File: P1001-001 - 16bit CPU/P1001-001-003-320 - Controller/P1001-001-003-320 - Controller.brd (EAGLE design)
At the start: 200 x 48 mm, 108 parts, among them IC1 74LS138D, IC10 74ALS00D, IC11 74ABT164D, IC12 74ABT164D, IC13 74ABT164D, IC14 74LS138D, IC15 74ABT164D, IC16 74ABT164D, IC17 74ABT164D, IC18 74ABT164D, IC19 74ABT164D, IC2 74LS157D, IC20 74ABT164D, IC3 74LS138D, IC4 74LS138D, IC5 74LS138D, IC6 74LS157D, IC7 74LS157D, IC8 74LS157D, IC9 74LS157D, J1 22-27-2041-04

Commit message: Add the control board
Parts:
- removed ALU_HIGH, ALU_LOW, A_OUT2, B_IN_LOW, B_OUT2, C_REG, RAN_IN_2, STACK: (no value), jumper:JP4
- removed A_CLEAR, B_CLEAR, D_IN, RAM_IN_LOW, X_SWAP: (no value), led:SFH482
- removed BACKBUS, FRONTBUS: (no value), con-harting-ml:ML16
- removed B_IN_HIGH, RAM_PC_OUT, RAN_IN_3: (no value), jumper:JP1
- removed D_REG, RAN_IN_1, X_REG: (no value), jumper:JP2W
- removed IC11, IC12, IC13, IC15, IC16, IC17, IC18, IC19, IC20: 74ABT164D, 74xx-us:SO14
- removed IC14: 74LS138D, 74xx-us:SO16
- removed IC2, IC6, IC7, IC8, IC9: 74LS157D, 74xx-us:SO16
- removed JP5: (no value), jumper:JP2
- removed U$2, U$3: SST39VF1602-70-4I-EKE, 16bit:TSOP48
- added ABC_CLEAR, B_IN_LOW1, HALT_RESEDT_NEXTINS, PC_MAR_IR_IN, RAM_STACK_IN: (no value), jumper:JP2W
- added ADD_HIGH, ADD_LOW, ADD_MID, BA_HIGH, BA_LOW, BB_HIGH, BB_LOW, BC_HIGH, BC_LOW: 74ABT164D, 74xx-us:SO14
- added ADD_SUB, B_IN_HIGH1, CLEAR_OUNS, EXTRA_1_2_PINS, EXTRA_3_4_PINS, EXTRA_5_6_PINS, INTERUPTS, PC_INC_DEC, RAM_IMT_OUT: (no value), jumper:JP1
- added A_CLEAR_LED, B_CLEAR_LED, D_CLEAR_LED, D_HIGH, D_IN_H, D_IN_L, D_LOW, EXTRA1, EXTRA2, EXTRA3, EXTRA4, EXTRA5, EXTRA6, EXTRA_OUT1, EXTRA_OUT2, EXTRA_OUT3, EXTRA_OUT4, INTERUPT_OUT, PAUSE_INERUPT, PC_DEC, PLAY_INTERUPT, RAM_IN_L, ROL, ROR, STEP1, STEP2, STEP3, STEP4: (no value), led:SFH482
- added A_OUT_PINS, B_OUT_PIMS, C_X_OC_STACK_OUT, D_OUT_PINS, EXTRA_OUT, IN_C_D_X, LOGIC_OP, SHIFT_ROLL, STACK_C, STEP_PINS: (no value), jumper:JP4
- added BANKA, BANKB, BANKC: SST39VF1602-70-4I-EKE, 16bit:TSOP48
- added IC21, IC22, IC23: 74LS138D, 74xx-us:SO16
- added IC27: MEGA8535-A, atmel:TQFP44
- added POWER_PINS, READ_WRITE: (no value), jumper:JP2
- added PULL_DOWN, R12, R13, R14: (no value), rcl:M0805
- added R10, R7, R8: (no value), resistor-bourns:SO16
- added RN2: (no value), resistor-dil:SOMC20
- added SV3: (no value), con-harting-ml:ML16
- added SV5: (no value), con-harting-ml:ML6
- added SW_PROD_1, SW_PROD_2, SW_PROD_3, SW_PROD_4, SW_PROD_5: 74LS157D, 74xx-us:SO16
- A_IN_LOW: device jumper:JP4 -> jumper:JP2W
- JP4: device jumper:JP1 -> jumper:JP3Q
- U$1: value SST39VF1602-70-4I-EKE -> 4-DIGIT-7-SEGMENT; device 16bit:TSOP48 -> ADAFRUIT:4-DIGIT-7-SEGMENT
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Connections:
- removed net A-CLEAR: A_CLEAR.K, A_IN_LOW.4, IC14.15
- removed net ADD: ADD.K, ALU_LOW.1, IC3.15
- removed net AND: ALU_HIGH.3, AND.K, IC3.9
- removed net A_HIGH: A_HIGH.K, A_OUT2.2, IC5.14
- removed net A_IN: A_IN.K, A_IN_LOW.3, IC14.14
- removed net A_IN_H_H: A_IN_H_H.K, A_IN_LOW.1, IC14.12
- removed net A_IN_H_L: A_IN_HIGH.1, A_IN_H_L.K, IC14.10
- removed net A_IN_L_H: A_IN_HIGH.2, A_IN_L_H.K, IC14.11
- removed net A_IN_L_L: A_IN_LOW.2, A_IN_L_L.K, IC14.13
- removed net A_LOW: A_LOW.K, A_OUT2.3, IC5.13
- removed net A_OUT: A_OUT.K, A_OUT2.4, IC5.12
- removed net A_SWAP: A_OUT2.1, A_SWAP.K, IC5.15
- removed net BUS0: BACKBUS.1, IC4.1, IC5.1
- removed net BUS1: BACKBUS.2, IC4.2, IC5.2
- removed net BUS10: BACKBUS.11, C_IN.K, C_REG.1
- removed net BUS11: BACKBUS.12, D_IN.K, D_REG.1
- removed net BUS12: BACKBUS.13, X_IN.K, X_REG.1
- removed net BUS13: BACKBUS.14, IR_IN.K, RAN_IN_3.2
- removed net BUS14: BACKBUS.15, MAR_IN.K, RAN_IN_3.1
- removed net BUS15: BACKBUS.16, PC_IN.K, RAN_IN_2.4
- removed net BUS16: FRONTBUS.1, RAM_IN_LOW.K, RAN_IN_2.3
- removed net BUS17: FRONTBUS.2, RAM_IN_H.K, RAN_IN_2.2
- removed net BUS18: FRONTBUS.3, IC3.1
- removed net BUS19: FRONTBUS.4, IC3.2
- removed net BUS2: BACKBUS.3, IC4.3, IC5.3
- removed net BUS20: FRONTBUS.5, IC3.3
- removed net BUS21: FRONTBUS.6, PC_INC.K, RAN_IN_2.1
- removed net BUS22: FRONTBUS.7, STACK.2, STACK_INC.K
- removed net BUS23: FRONTBUS.8, STACK.3, STACK_DEC.K
- removed net BUS24: C_INC.K, C_REG.2, FRONTBUS.9
- removed net BUS25: C_DEC.K, C_REG.3, FRONTBUS.10
- removed net BUS26: FRONTBUS.11, RAN_IN_1.3, RESET.K
- removed net BUS27: FRONTBUS.12, HALT.K, RAN_IN_1.2
- removed net BUS28: FRONTBUS.13, NEXT_INS.K, RAN_IN_1.1
- removed net BUS29: FRONTBUS.14, STACK.1, STACK_IN.K
- removed net BUS3: BACKBUS.4, IC4.4, IC5.4
- removed net BUS30: FRONTBUS.15
- removed net BUS31: FRONTBUS.16
- removed net BUS4: BACKBUS.5, IC14.1
- removed net BUS5: BACKBUS.6, IC14.2
- removed net BUS6: BACKBUS.7, IC14.3
- removed net BUS7: BACKBUS.8, IC1.1
- removed net BUS8: BACKBUS.9, IC1.2
- removed net BUS9: BACKBUS.10, IC1.3
- removed net B_CLEAR: B_CLEAR.K, B_IN_LOW.4, IC1.15
- removed net B_HIGH: B_HIGH.K, B_OUT2.2, IC5.10
- removed net B_IN: B_IN.K, B_IN_LOW.3, IC1.14
- removed net B_IN_H_H: B_IN_H_H.K, B_IN_LOW.1, IC1.12
- removed net B_IN_H_L: B_IN_HIGH.1, B_IN_H_L.K, IC1.10
- removed net B_IN_L_H: B_IN_HIGH.2, B_IN_L_H.K, IC1.11
- removed net B_IN_L_L: B_IN_LOW.2, B_IN_L_L.K, IC1.13
- removed net B_LOW: B_LOW.K, B_OUT2.3, IC5.9
- removed net B_OUT: B_OUT.K, B_OUT2.4, IC5.7
- removed net B_SWAP: B_OUT2.1, B_SWAP.K, IC5.11
- removed net HALT_LED: NEXT_INS.A, R3.13
- removed net NOT: ALU_HIGH.1, IC3.11, NOT.K
- removed net OR: ALU_HIGH.2, IC3.10, OR.K
- removed net PC_OUT: IC4.14, PC_OUT.K
- removed net RAM_OUT: IC4.9, RAM_OUT.K
- removed net SHL: ALU_LOW.3, IC3.13, SHL.K
- removed net SHR: ALU_LOW.4, IC3.12, SHR.K
- removed net SUB: ALU_LOW.2, IC3.14, SUB.K
- removed net XOR: ALU_HIGH.4, IC3.7, XOR.K
- new net A: IC27.37, RN2.20
- new net B: IC27.36, RN2.19
- new net BANKA_PROG: BANKA.11, JP4.5, R12.1
- new net BANKB_PROG: BANKB.11, JP4.3, R13.1
- new net BANKC_PROG: BANKC.11, JP4.1, R14.1
- new net C: IC27.35, RN2.18
- new net D: IC27.34, RN2.17
- new net DIG0: IC27.40, U$1.PIN14
- new net DIG1: IC27.41, U$1.PIN11
- new net DIG2: IC27.42, U$1.PIN10
- new net DIG3: IC27.43, U$1.PIN6
- new net DP: IC27.30, RN2.13
- new net E: IC27.33, RN2.16
- new net EXTERN_BUS0: IC27.9, R10.1, SV3.1
- new net EXTERN_BUS1: IC27.10, R10.9, SV3.2
- new net EXTERN_BUS10: IC27.21, R10.6, SV3.11
- new net EXTERN_BUS11: IC27.22, R10.14, SV3.12
- new net EXTERN_BUS12: IC27.23, R10.7, SV3.13
- new net EXTERN_BUS13: IC27.24, R10.15, SV3.14
- new net EXTERN_BUS14: IC27.25, R10.8, SV3.15
- new net EXTERN_BUS15: IC27.26, PULL_DOWN.1, SV3.16
- new net EXTERN_BUS2: IC27.11, R10.2, SV3.3
- new net EXTERN_BUS3: IC27.12, R10.10, SV3.4
- new net EXTERN_BUS4: IC27.13, R10.3, SV3.5
- new net EXTERN_BUS5: IC27.14, R10.11, SV3.6
- new net EXTERN_BUS6: IC27.15, R10.4, SV3.7
- new net EXTERN_BUS7: IC27.16, R10.12, SV3.8
- new net EXTERN_BUS8: IC27.19, R10.5, SV3.9
- new net EXTERN_BUS9: IC27.20, R10.13, SV3.10
- new net F: IC27.32, RN2.15
- new net G: IC27.31, RN2.14
- new net N$100: D_OUT.A, R3.14
- new net N$101: D_LOW.A, R3.13
- new net N$102: D_HIGH.A, R3.12
- new net N$103: D_SWAP.A, R3.11
- new net N$104: R3.10, X_OUT.A
- new net N$105: PC_OUT.A, R3.9
- new net N$106: IC5.15, RAM_IMT_OUT.1, RAM_OUT.K
- new net N$107: IC5.14, INTERUPT_OUT.K, RAM_IMT_OUT.2
- new net N$108: EXTRA_OUT.4, EXTRA_OUT1.K, IC5.13
- new net N$109: EXTRA_OUT.3, EXTRA_OUT2.K, IC5.12
- new net N$110: EXTRA_OUT.2, EXTRA_OUT3.K, IC5.11
- new net N$111: EXTRA_OUT.1, EXTRA_OUT4.K, IC5.10
- new net N$112: R2.1, STACK_OUT.A
- new net N$113: EXTRA_OUT4.A, R2.8
- new net N$114: EXTRA_OUT3.A, R2.7
- new net N$115: EXTRA_OUT2.A, R2.6
- new net N$116: EXTRA_OUT1.A, R2.5
- new net N$117: R2.2, RAM_OUT.A
- new net N$118: INTERUPT_OUT.A, R2.3
- new net N$119: IC27.1, SV5.3
- new net N$120: IC27.3, SV5.4
- new net N$121: IC27.2, SV5.6
- new net N$122: IC27.4, SV5.2
- new net N$123: RN2.1, U$1.PIN13
- new net N$124: RN2.2, U$1.PIN9
- new net N$125: RN2.3, U$1.PIN4
- new net N$126: RN2.4, U$1.PIN2
- new net N$127: RN2.5, U$1.PIN1
- new net N$128: RN2.6, U$1.PIN12
- new net N$129: RN2.7, U$1.PIN5
- new net N$130: RN2.8, U$1.PIN3
- new net N$131: R2.15, STEP1.A
- new net N$132: R2.14, STEP2.A
- new net N$133: R2.13, STEP3.A
- new net N$134: R2.12, STEP4.A
- new net N$37: BANKA.27, BANKA.46, BANKB.27, BANKB.46, BANKC.27, BANKC.46
- new net N$42: BANKA.28, BANKB.28, BANKC.28, READ_WRITE.2
- new net N$43: EXTRA5.A, R8.5
- new net N$63: IC1.13, SHIFT_ROLL.4, SHL.K
- new net N$64: IC1.12, SHIFT_ROLL.3, SHR.K
- new net N$65: IC1.11, ROL.K, SHIFT_ROLL.2
- new net N$66: IC1.10, ROR.K, SHIFT_ROLL.1
- new net N$67: NOT.A, R7.9
- new net N$68: AND.A, R7.10
- new net N$69: OR.A, R7.11
- new net N$70: R7.12, XOR.A
- new net N$71: IC23.7, LOGIC_OP.1, XOR.K
- new net N$72: IC23.9, LOGIC_OP.2, OR.K
- new net N$73: AND.K, IC23.10, LOGIC_OP.3
- new net N$74: IC23.11, LOGIC_OP.4, NOT.K
- new net N$75: A_OUT.K, A_OUT_PINS.1, IC3.15
- new net N$76: A_LOW.K, A_OUT_PINS.2, IC3.14
- new net N$77: A_HIGH.K, A_OUT_PINS.3, IC3.13
- new net N$78: A_OUT_PINS.4, A_SWAP.K, IC3.12
- new net N$79: B_OUT.K, B_OUT_PIMS.1, IC3.11
- new net N$80: B_LOW.K, B_OUT_PIMS.2, IC3.10
- new net N$81: B_HIGH.K, B_OUT_PIMS.3, IC3.9
- new net N$82: B_OUT_PIMS.4, B_SWAP.K, IC3.7
- new net N$83: D_OUT.K, D_OUT_PINS.1, IC4.14
- new net N$84: C_OUT.K, C_X_OC_STACK_OUT.4, IC4.15
- new net N$85: D_LOW.K, D_OUT_PINS.2, IC4.13
- new net N$86: D_HIGH.K, D_OUT_PINS.3, IC4.12
- new net N$87: D_OUT_PINS.4, D_SWAP.K, IC4.11
- new net N$88: C_X_OC_STACK_OUT.3, IC4.10, X_OUT.K
- new net N$89: C_X_OC_STACK_OUT.2, IC4.9, PC_OUT.K
- new net N$90: C_X_OC_STACK_OUT.1, IC4.7, STACK_OUT.K
- new net N$91: A_OUT.A, R3.1
- new net N$92: A_LOW.A, R3.2
- new net N$93: A_HIGH.A, R3.3
- new net N$94: A_SWAP.A, R3.4
- new net N$95: B_OUT.A, R3.5
- new net N$96: B_LOW.A, R3.6
- new net N$97: B_HIGH.A, R3.7
- new net N$98: B_SWAP.A, R3.8
- new net N$99: C_OUT.A, R3.15
- new net WRITE_ENABLE: BANKA.14, BANKB.14, BANKC.14, JP3.2
- net !CLEAR: now also BANKA.12, BANKB.12, BANKC.12, CLEAR_OUNS.1; no longer JP4.1
- net ADDR_BUS0: now also BANKA.25, BANKB.25, BANKC.25, SW_PROD_1.12; no longer IC7.12, U$1.25, U$2.25, U$3.25
- net ADDR_BUS1: now also BANKA.24, BANKB.24, BANKC.24, SW_PROD_1.9; no longer IC7.9, U$1.24, U$2.24, U$3.24
- net ADDR_BUS10: now also BANKA.6, BANKB.6, BANKC.6, SW_PROD_3.7; no longer IC2.7, U$1.6, U$2.6, U$3.6
- net ADDR_BUS11: now also BANKA.5, BANKB.5, BANKC.5, SW_PROD_3.4; no longer IC2.4, U$1.5, U$2.5, U$3.5
- net ADDR_BUS12: now also BANKA.4, BANKB.4, BANKC.4, SW_PROD_4.4; no longer IC8.4, U$1.4, U$2.4, U$3.4
- net ADDR_BUS13: now also BANKA.3, BANKB.3, BANKC.3, SW_PROD_4.7; no longer IC8.7, U$1.3, U$2.3, U$3.3
- net ADDR_BUS14: now also BANKA.2, BANKB.2, BANKC.2, SW_PROD_4.9; no longer IC8.9, U$1.2, U$2.2, U$3.2
- net ADDR_BUS15: now also BANKA.1, BANKB.1, BANKC.1, SW_PROD_4.12; no longer IC8.12, U$1.1, U$2.1, U$3.1
- net ADDR_BUS16: now also BANKA.48, BANKB.48, BANKC.48, SW_PROD_5.4; no longer IC9.4, U$1.48, U$2.48, U$3.48
- net ADDR_BUS17: now also BANKA.17, BANKB.17, BANKC.17, SW_PROD_5.7; no longer IC9.7, U$1.17, U$2.17, U$3.17
- net ADDR_BUS18: now also BANKA.16, BANKB.16, BANKC.16, SW_PROD_5.9; no longer IC9.9, U$1.16, U$2.16, U$3.16
- net ADDR_BUS19: now also BANKA.9, BANKB.9, BANKC.9, SW_PROD_5.12; no longer IC9.12, U$1.9, U$2.9, U$3.9
- net ADDR_BUS2: now also BANKA.23, BANKB.23, BANKC.23, SW_PROD_1.7; no longer IC7.7, U$1.23, U$2.23, U$3.23
- net ADDR_BUS3: now also BANKA.22, BANKB.22, BANKC.22, SW_PROD_1.4; no longer IC7.4, U$1.22, U$2.22, U$3.22
- net ADDR_BUS4: now also BANKA.21, BANKB.21, BANKC.21, SW_PROD_2.12; no longer IC6.12, U$1.21, U$2.21, U$3.21
- net ADDR_BUS5: now also BANKA.20, BANKB.20, BANKC.20, SW_PROD_2.9; no longer IC6.9, U$1.20, U$2.20, U$3.20
- net ADDR_BUS6: now also BANKA.19, BANKB.19, BANKC.19, SW_PROD_2.7; no longer IC6.7, U$1.19, U$2.19, U$3.19
- net ADDR_BUS7: now also BANKA.18, BANKB.18, BANKC.18, SW_PROD_2.4; no longer IC6.4, U$1.18, U$2.18, U$3.18
- net ADDR_BUS8: now also BANKA.8, BANKB.8, BANKC.8, SW_PROD_3.12; no longer IC2.12, U$1.8, U$2.8, U$3.8
- net ADDR_BUS9: now also BANKA.7, BANKB.7, BANKC.7, SW_PROD_3.9; no longer IC2.9, U$1.7, U$2.7, U$3.7
- net ADDR_SHIFT: now also ADD_LOW.1, ADD_LOW.2; no longer IC11.1, IC11.2
- net CLEAR: now also CLEAR_OUNS.2; no longer JP4.2
- net CLK: now also POWER_PINS.1; no longer JP5.1
- net DATAA0: now also BANKA.29, BA_LOW.3, IC3.1, IC4.1, IC5.1; no longer IC15.3, U$1.29
- net DATAA1: now also BANKA.31, BA_LOW.4, IC3.2, IC4.2, IC5.2; no longer IC15.4, U$1.31
- net DATAA10: now also BANKA.34, BA_HIGH.5, EXTRA6.K, EXTRA_5_6_PINS.2; no longer IC16.5, U$1.34
- net DATAA11: now also ABC_CLEAR.1, A_CLEAR_LED.K, BANKA.36, BA_HIGH.6; no longer IC16.6, U$1.36
- net DATAA12: now also ABC_CLEAR.2, BANKA.39, BA_HIGH.10, B_CLEAR_LED.K; no longer IC16.10, U$1.39
- net DATAA13: now also ABC_CLEAR.3, BANKA.41, BA_HIGH.11, D_CLEAR_LED.K; no longer IC16.11, U$1.41
- net DATAA14: now also BANKA.43, BA_HIGH.12, INTERUPTS.1, PAUSE_INERUPT.K; no longer IC16.12, U$1.43
- net DATAA15: now also BANKA.45, BA_HIGH.13, INTERUPTS.2, PLAY_INTERUPT.K; no longer IC16.13, U$1.45
- net DATAA2: now also BANKA.33, BA_LOW.5, IC3.3, IC4.3, IC5.3; no longer IC15.5, U$1.33
- net DATAA3: now also BANKA.35, BA_LOW.6, IC3.4, IC4.4, IC5.4; no longer IC15.6, U$1.35
- net DATAA4: now also BANKA.38, BA_LOW.10, IC3.5, IC4.5, IC5.5; no longer IC15.10, U$1.38
- net DATAA5: now also BANKA.40, BA_LOW.11, EXTRA1.K, EXTRA_1_2_PINS.1; no longer IC15.11, U$1.40
- net DATAA6: now also BANKA.42, BA_LOW.12, EXTRA2.K, EXTRA_1_2_PINS.2; no longer IC15.12, U$1.42
- net DATAA7: now also BANKA.44, BA_HIGH.1, BA_HIGH.2, BA_LOW.13, EXTRA3.K, EXTRA_3_4_PINS.1; no longer IC15.13, IC16.1, IC16.2, U$1.44
- net DATAA8: now also BANKA.30, BA_HIGH.3, EXTRA4.K, EXTRA_3_4_PINS.2; no longer IC16.3, U$1.30
- net DATAA9: now also BANKA.32, BA_HIGH.4, EXTRA5.K, EXTRA_5_6_PINS.1; no longer IC16.4, U$1.32
- net DATAA_SHIFT: now also BA_LOW.1, BA_LOW.2; no longer IC15.1, IC15.2
- net DATAB0: now also BANKB.29, BB_LOW.3, IC21.1; no longer IC17.3, U$2.29
- net DATAB1: now also BANKB.31, BB_LOW.4, IC21.2; no longer IC17.4, U$2.31
- net DATAB10: now also BANKB.34, BB_HIGH.5, IR_IN.K, PC_MAR_IR_IN.1; no longer IC18.5, U$2.34
- net DATAB11: now also BANKB.36, BB_HIGH.6, MAR_IN.K, PC_MAR_IR_IN.2; no longer IC18.6, U$2.36
- net DATAB12: now also BANKB.39, BB_HIGH.10, PC_IN.K, PC_MAR_IR_IN.3; no longer IC18.10, U$2.39
- net DATAB13: now also BANKB.41, BB_HIGH.11, RAM_STACK_IN.1, STACK_IN.K; no longer IC18.11, U$2.41
- net DATAB14: now also BANKB.43, BB_HIGH.12, RAM_IN_L.K, RAM_STACK_IN.2; no longer IC18.12, U$2.43
- net DATAB15: now also BANKB.45, BB_HIGH.13, RAM_IN_H.K, RAM_STACK_IN.3; no longer IC18.13, U$2.45
- net DATAB2: now also BANKB.33, BB_LOW.5, IC21.3; no longer IC17.5, U$2.33
- net DATAB3: now also BANKB.35, BB_LOW.6, IC22.1; no longer IC17.6, U$2.35
- net DATAB4: now also BANKB.38, BB_LOW.10, IC22.2, PC_INC_DEC.2; no longer IC17.10, U$2.38
- net DATAB5: now also BANKB.40, BB_LOW.11, IC22.3; no longer IC17.11, U$2.40
- net DATAB6: now also BANKB.42, BB_LOW.12, C_IN.K, IN_C_D_X.1; no longer IC17.12, U$2.42
- net DATAB7: now also BANKB.44, BB_HIGH.1, BB_HIGH.2, BB_LOW.13, D_IN_L.K, IN_C_D_X.2; no longer IC17.13, IC18.1, IC18.2, U$2.44
- net DATAB8: now also BANKB.30, BB_HIGH.3, D_IN_H.K, IN_C_D_X.3; no longer IC18.3, U$2.30
- net DATAB9: now also BANKB.32, BB_HIGH.4, IN_C_D_X.4, X_IN.K; no longer IC18.4, U$2.32
- net DATAB_SHIFT: now also BB_LOW.1, BB_LOW.2; no longer IC17.1, IC17.2
- net DATAC0: now also BANKC.29, BC_LOW.3, IC1.1, IC23.1; no longer IC19.3, U$3.29
- net DATAC1: now also BANKC.31, BC_LOW.4, IC1.2, IC23.2; no longer IC19.4, U$3.31
- net DATAC10: now also BANKC.34, BC_HIGH.5; no longer IC20.5, U$3.34
- net DATAC11: now also BANKC.36, BC_HIGH.6; no longer IC20.6, U$3.36
- net DATAC12: now also BANKC.39, BC_HIGH.10; no longer IC20.10, U$3.39
- net DATAC13: now also BANKC.41, BC_HIGH.11, HALT_RESEDT_NEXTINS.3, RESET.K; no longer IC20.11, U$3.41
- net DATAC14: now also BANKC.43, BC_HIGH.12, HALT.K, HALT_RESEDT_NEXTINS.2; no longer IC20.12, U$3.43
- net DATAC15: now also BANKC.45, BC_HIGH.13, HALT_RESEDT_NEXTINS.1, NEXT_INS.K; no longer IC20.13, U$3.45
- net DATAC2: now also BANKC.33, BC_LOW.5, IC1.3, IC23.3; no longer IC19.5, U$3.33
- net DATAC3: now also BANKC.35, BC_LOW.6, IC1.4, IC23.4; no longer IC19.6, U$3.35
- net DATAC4: now also BANKC.38, BC_LOW.10, PC_DEC.K; no longer IC19.10, U$3.38
- net DATAC5: now also BANKC.40, BC_LOW.11, PC_INC.K, PC_INC_DEC.1; no longer IC19.11, U$3.40
- net DATAC6: now also BANKC.42, BC_LOW.12, STACK_C.4, STACK_INC.K; no longer IC19.12, U$3.42
- net DATAC7: now also BANKC.44, BC_HIGH.1, BC_HIGH.2, BC_LOW.13, STACK_C.3, STACK_DEC.K; no longer IC19.13, IC20.1, IC20.2, U$3.44
- net DATAC8: now also BANKC.30, BC_HIGH.3, C_INC.K, STACK_C.2; no longer IC20.3, U$3.30
- net DATAC9: now also BANKC.32, BC_HIGH.4, C_DEC.K, STACK_C.1; no longer IC20.4, U$3.32
- net DATAC_SHIFT: now also BC_LOW.1, BC_LOW.2; no longer IC19.1, IC19.2
- net DATA_ADDR_CLOCK: now also BA_HIGH.8, BA_LOW.8, BB_HIGH.8, BB_LOW.8, BC_HIGH.8, BC_LOW.8; no longer IC15.8, IC16.8, IC17.8, IC18.8, IC19.8, IC20.8
- net GND: now also ADD_HIGH.7, ADD_LOW.7, ADD_MID.7, BANKA.26, BANKA.37, BANKB.26, BANKB.37, BANKC.26, BANKC.37, BA_HIGH.7, BA_LOW.7, BB_HIGH.7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; no longer IC1.4, IC11.7, IC12.7, IC13.7, IC14.4, IC14.5, IC14.8, IC15.7, IC16.7, IC17.7, IC18.7, IC19.7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
- net IN_BUS0: now also STEP1.K, STEP_PINS.1, SW_PROD_1.14; no longer IC7.14
- net IN_BUS1: now also STEP2.K, STEP_PINS.2, SW_PROD_1.11; no longer IC7.11
- net IN_BUS10: now also SW_PROD_3.5; no longer IC2.5
- net IN_BUS11: now also SW_PROD_3.2; no longer IC2.2
- net IN_BUS12: now also SW_PROD_4.2; no longer IC8.2
- net IN_BUS13: now also SW_PROD_4.5; no longer IC8.5
- net IN_BUS14: now also SW_PROD_4.11; no longer IC8.11
- net IN_BUS15: now also SW_PROD_4.14; no longer IC8.14
- net IN_BUS16: now also SW_PROD_5.2; no longer IC9.2
- net IN_BUS17: now also SW_PROD_5.5; no longer IC9.5
- net IN_BUS18: now also SW_PROD_5.11; no longer IC9.11
- net IN_BUS19: now also SW_PROD_5.14; no longer IC9.14
- net IN_BUS2: now also STEP3.K, STEP_PINS.3, SW_PROD_1.5; no longer IC7.5
- net IN_BUS3: now also STEP4.K, STEP_PINS.4, SW_PROD_1.2; no longer IC7.2
- net IN_BUS4: now also SW_PROD_2.14; no longer IC6.14
- net IN_BUS5: now also SW_PROD_2.11; no longer IC6.11
- net IN_BUS6: now also SW_PROD_2.5; no longer IC6.5
- net IN_BUS7: now also SW_PROD_2.2; no longer IC6.2
- net IN_BUS8: now also SW_PROD_3.14; no longer IC2.14
- net IN_BUS9: now also SW_PROD_3.11; no longer IC2.11
- net N$10: now also D_CLEAR_LED.A, R8.9; no longer IC4.11, X_REG.2, X_SWAP.K
- net N$11: now also PAUSE_INERUPT.A, R8.10; no longer R3.2, X_IN.A
- net N$12: now also PLAY_INTERUPT.A, R8.11; no longer IC4.7, X_OUT.K, X_REG.3
- net N$13: now also C_IN.A, R8.12; no longer R3.15, X_OUT.A
- net N$14: now also D_IN_L.A, R8.15; no longer R3.9, STACK_IN.A
- net N$15: now also D_IN_H.A, R8.14; no longer R3.10, STACK_INC.A
- net N$16: now also PC_INC.A, R5.1; no longer R3.11, STACK_DEC.A
- net N$17: now also PC_DEC.A, R5.2; no longer R3.12, STACK_OUT.A
- net N$18: now also IR_IN.A, R5.3; no longer IC4.13, STACK.4, STACK_OUT.K
- net N$19: now also MAR_IN.A, R5.4; no longer D_REG.2, D_SWAP.K, IC4.15
- net N$2: now also EXTRA1.A, R8.1; no longer C_IN.A, R3.8
- net N$20: now also PC_IN.A, R5.5; no longer D_SWAP.A, R3.14
- net N$21: now also R5.6, STACK_IN.A; no longer A_CLEAR.A, R5.9
- net N$22: now also R5.7, RAM_IN_L.A; no longer ADD.A, R5.1
- net N$23: now also R5.8, RAM_IN_H.A; no longer A_IN.A, R5.10
- net N$24: now also NEXT_INS.A, R5.10; no longer B_CLEAR.A, R4.9
- net N$25: now also R5.15, STACK_DEC.A; no longer B_IN.A, R4.10
- net N$26: now also C_INC.A, R5.14; no longer B_IN_L_L.A, R4.11
- net N$27: now also C_DEC.A, R5.13; no longer B_IN_H_H.A, R4.12
- net N$28: now also R5.12, RESET.A; no longer R5.8, XOR.A
- net N$29: now also HALT.A, R5.11; no longer AND.A, R5.7
- net N$3: now also EXTRA2.A, R8.2; no longer C_OUT.K, C_REG.4, IC4.10
- net N$30: now also R5.9, STACK_INC.A; no longer OR.A, R5.6
- net N$31: now also A_IN.K, A_IN_LOW.1, IC21.15; no longer NOT.A, R5.5
- net N$32: now also A_IN_LOW.2, A_IN_L_L.K, IC21.14; no longer R5.4, SHR.A
- net N$33: now also A_IN_H_H.K, A_IN_LOW.3, IC21.13; no longer R5.3, SHL.A
- net N$34: now also A_IN_HIGH.1, A_IN_L_H.K, IC21.12; no longer R5.2, SUB.A
- net N$35: now also A_IN_HIGH.2, A_IN_H_L.K, IC21.11; no longer B_IN_L_H.A, R4.13
- net N$36: now also A_IN.A, R4.8; no longer B_IN_H_L.A, R4.14
- net N$38: now also R4.7; no longer R5.11
- net N$39: now also R4.6; no longer R5.12
- net N$4: now also R8.13, X_IN.A; no longer C_OUT.A, R3.5
- net N$40: now also R4.5; no longer R5.13
- net N$41: now also R4.4; no longer R5.14
- net N$44: now also B_IN.A, B_IN_LOW1.3, IC22.15; no longer R2.15, RAM_OUT.A, RAM_PC_OUT.2
- net N$45: now also B_IN_LOW1.2, B_IN_L_L.A, IC22.14; no longer A_SWAP.A, R2.1
- net N$46: now also B_IN_H_H.A, B_IN_LOW1.1, IC22.13; no longer A_HIGH.A, R2.2
- net N$47: now also B_IN_HIGH1.2, B_IN_L_H.A, IC22.12; no longer A_LOW.A, R2.3
- net N$48: now also B_IN_HIGH1.1, B_IN_H_L.A, IC22.11; no longer A_OUT.A, R2.4
- net N$49: now also B_IN.K, R4.9; no longer B_SWAP.A, R2.5
- net N$5: now also EXTRA4.A, R8.4; no longer C_DEC.A, R3.6
- net N$51: now also B_IN_L_L.K, R4.10; no longer B_HIGH.A, R2.6
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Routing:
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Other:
- board size 200 x 48 mm -> 200 x 152 mm

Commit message: Controller done?
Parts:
- removed ADD_HIGH, ADD_LOW, ADD_MID, BA_HIGH, BA_LOW, BB_HIGH, BB_LOW, BC_HIGH, BC_LOW: 74ABT164D, 74xx-us:SO14
- removed JP4: (no value), jumper:JP3Q
- removed R12, R13, R14: (no value), rcl:M0805
- removed READ_WRITE: (no value), jumper:JP2
- removed SW_PROD_1, SW_PROD_2, SW_PROD_3, SW_PROD_4, SW_PROD_5: 74LS157D, 74xx-us:SO16
- added SV2: (no value), con-harting-ml:ML6
- BANKA, BANKB, BANKC: value SST39VF1602-70-4I-EKE -> (none); device 16bit:TSOP48 -> con-harting-ml:ML16
- JP3: device jumper:JP6Q -> pinhead:1X20
- moved JP3 103.7 mm to (102.9, 122.2), turned to 0 degrees
- moved BANKC 89.6 mm to (120.6, 100.0)
- moved IC3 78.3 mm to (19.0, 121.0)
- moved BANKB 72.1 mm to (100.3, 100.0)
- moved BANKA 62.6 mm to (80.0, 100.0)
- moved R5 39.1 mm to (150.0, 80.0)
- moved R7 20.4 mm to (110.0, 80.0)
- moved R2 17.5 mm to (130.0, 80.0)
- moved U$4 16.2 mm to (140.0, 133.0)
- moved R8 6.71 mm to (90.0, 80.0)
- moved R3 4.24 mm to (70.0, 80.0)
- moved R4 4.24 mm to (50.0, 80.0)
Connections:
- removed net ADDR_BUS0: BANKA.25, BANKB.25, BANKC.25, SW_PROD_1.12
- removed net ADDR_BUS1: BANKA.24, BANKB.24, BANKC.24, SW_PROD_1.9
- removed net ADDR_BUS10: BANKA.6, BANKB.6, BANKC.6, SW_PROD_3.7
- removed net ADDR_BUS11: BANKA.5, BANKB.5, BANKC.5, SW_PROD_3.4
- removed net ADDR_BUS12: BANKA.4, BANKB.4, BANKC.4, SW_PROD_4.4
- removed net ADDR_BUS13: BANKA.3, BANKB.3, BANKC.3, SW_PROD_4.7
- removed net ADDR_BUS14: BANKA.2, BANKB.2, BANKC.2, SW_PROD_4.9
- removed net ADDR_BUS15: BANKA.1, BANKB.1, BANKC.1, SW_PROD_4.12
- removed net ADDR_BUS16: BANKA.48, BANKB.48, BANKC.48, SW_PROD_5.4
- removed net ADDR_BUS17: BANKA.17, BANKB.17, BANKC.17, SW_PROD_5.7
- removed net ADDR_BUS18: BANKA.16, BANKB.16, BANKC.16, SW_PROD_5.9
- removed net ADDR_BUS19: BANKA.9, BANKB.9, BANKC.9, SW_PROD_5.12
- removed net ADDR_BUS2: BANKA.23, BANKB.23, BANKC.23, SW_PROD_1.7
- removed net ADDR_BUS3: BANKA.22, BANKB.22, BANKC.22, SW_PROD_1.4
- removed net ADDR_BUS4: BANKA.21, BANKB.21, BANKC.21, SW_PROD_2.12
- removed net ADDR_BUS5: BANKA.20, BANKB.20, BANKC.20, SW_PROD_2.9
- removed net ADDR_BUS6: BANKA.19, BANKB.19, BANKC.19, SW_PROD_2.7
- removed net ADDR_BUS7: BANKA.18, BANKB.18, BANKC.18, SW_PROD_2.4
- removed net ADDR_BUS8: BANKA.8, BANKB.8, BANKC.8, SW_PROD_3.12
- removed net ADDR_BUS9: BANKA.7, BANKB.7, BANKC.7, SW_PROD_3.9
- removed net ADDR_SHIFT: ADD_LOW.1, ADD_LOW.2, JP3.5
- removed net BANKA_PROG: BANKA.11, JP4.5, R12.1
- removed net BANKB_PROG: BANKB.11, JP4.3, R13.1
- removed net BANKC_PROG: BANKC.11, JP4.1, R14.1
- removed net DATAA_SHIFT: BA_LOW.1, BA_LOW.2, JP3.6
- removed net DATAB_SHIFT: BB_LOW.1, BB_LOW.2, JP3.4
- removed net DATAC_SHIFT: BC_LOW.1, BC_LOW.2, JP3.3
- removed net DATA_ADDR_CLOCK: BA_HIGH.8, BA_LOW.8, BB_HIGH.8, BB_LOW.8, BC_HIGH.8, BC_LOW.8, JP3.7
- removed net N$37: BANKA.27, BANKA.46, BANKB.27, BANKB.46, BANKC.27, BANKC.46
- removed net N$42: BANKA.28, BANKB.28, BANKC.28, READ_WRITE.2
- removed net PROGRAM: JP3.9, JP4.2, JP4.4, JP4.6
- removed net PROG_ADDR0: ADD_LOW.3, SW_PROD_1.13
- removed net PROG_ADDR1: ADD_LOW.4, SW_PROD_1.10
- removed net PROG_ADDR10: ADD_MID.5, SW_PROD_3.6
- removed net PROG_ADDR11: ADD_MID.6, SW_PROD_3.3
- removed net PROG_ADDR12: ADD_MID.10, SW_PROD_4.3
- removed net PROG_ADDR13: ADD_MID.11, SW_PROD_4.6
- removed net PROG_ADDR14: ADD_MID.12, SW_PROD_4.10
- removed net PROG_ADDR15: ADD_HIGH.1, ADD_HIGH.2, ADD_MID.13, SW_PROD_4.13
- removed net PROG_ADDR16: ADD_HIGH.3, SW_PROD_5.3
- removed net PROG_ADDR17: ADD_HIGH.4, SW_PROD_5.6
- removed net PROG_ADDR18: ADD_HIGH.5, SW_PROD_5.10
- removed net PROG_ADDR19: ADD_HIGH.6, SW_PROD_5.13
- removed net PROG_ADDR2: ADD_LOW.5, SW_PROD_1.6
- removed net PROG_ADDR3: ADD_LOW.6, SW_PROD_1.3
- removed net PROG_ADDR4: ADD_LOW.10, SW_PROD_2.13
- removed net PROG_ADDR5: ADD_LOW.11, SW_PROD_2.10
- removed net PROG_ADDR6: ADD_LOW.12, SW_PROD_2.6
- removed net PROG_ADDR7: ADD_LOW.13, ADD_MID.1, ADD_MID.2, SW_PROD_2.3
- removed net PROG_ADDR8: ADD_MID.3, SW_PROD_3.13
- removed net PROG_ADDR9: ADD_MID.4, SW_PROD_3.10
- removed net PROG_ADDR_CLOCK: ADD_HIGH.8, ADD_LOW.8, ADD_MID.8, JP3.8
- removed net PROG_CLEAR: ADD_HIGH.9, ADD_LOW.9, ADD_MID.9, BA_HIGH.9, BA_LOW.9, BB_HIGH.9, BB_LOW.9, BC_HIGH.9, BC_LOW.9, JP3.10
- removed net PROG_DIR: JP3.1, SW_PROD_1.1, SW_PROD_2.1, SW_PROD_3.1, SW_PROD_4.1, SW_PROD_5.1
- removed net WRITE_ENABLE: BANKA.14, BANKB.14, BANKC.14, JP3.2
- net !CLEAR: no longer BANKA.12, BANKB.12, BANKC.12
- net DATAA0: now also BANKA.1; no longer BANKA.29, BA_LOW.3
- net DATAA1: now also BANKA.2; no longer BANKA.31, BA_LOW.4
- net DATAA10: now also BANKA.11; no longer BANKA.34, BA_HIGH.5
- net DATAA11: now also BANKA.12; no longer BANKA.36, BA_HIGH.6
- net DATAA12: now also BANKA.13; no longer BANKA.39, BA_HIGH.10
- net DATAA13: now also BANKA.14; no longer BANKA.41, BA_HIGH.11
- net DATAA14: now also BANKA.15; no longer BANKA.43, BA_HIGH.12
- net DATAA15: now also BANKA.16; no longer BANKA.45, BA_HIGH.13
- net DATAA2: now also BANKA.3; no longer BANKA.33, BA_LOW.5
- net DATAA3: now also BANKA.4; no longer BANKA.35, BA_LOW.6
- net DATAA4: now also BANKA.5; no longer BANKA.38, BA_LOW.10
- net DATAA5: now also BANKA.6; no longer BANKA.40, BA_LOW.11
- net DATAA6: now also BANKA.7; no longer BANKA.42, BA_LOW.12
- net DATAA7: now also BANKA.8; no longer BANKA.44, BA_HIGH.1, BA_HIGH.2, BA_LOW.13
- net DATAA8: now also BANKA.9; no longer BANKA.30, BA_HIGH.3
- net DATAA9: now also BANKA.10; no longer BANKA.32, BA_HIGH.4
- net DATAB0: now also BANKB.1; no longer BANKB.29, BB_LOW.3
- net DATAB1: now also BANKB.2; no longer BANKB.31, BB_LOW.4
- net DATAB10: now also BANKB.11; no longer BANKB.34, BB_HIGH.5
- net DATAB11: now also BANKB.12; no longer BANKB.36, BB_HIGH.6
- net DATAB12: now also BANKB.13; no longer BANKB.39, BB_HIGH.10
- net DATAB13: now also BANKB.14; no longer BANKB.41, BB_HIGH.11
- net DATAB14: now also BANKB.15; no longer BANKB.43, BB_HIGH.12
- net DATAB15: now also BANKB.16; no longer BANKB.45, BB_HIGH.13
- net DATAB2: now also BANKB.3; no longer BANKB.33, BB_LOW.5
- net DATAB3: now also BANKB.4; no longer BANKB.35, BB_LOW.6
- net DATAB4: now also BANKB.5; no longer BANKB.38, BB_LOW.10
- net DATAB5: now also BANKB.6; no longer BANKB.40, BB_LOW.11
- net DATAB6: now also BANKB.7; no longer BANKB.42, BB_LOW.12
- net DATAB7: now also BANKB.8; no longer BANKB.44, BB_HIGH.1, BB_HIGH.2, BB_LOW.13
- net DATAB8: now also BANKB.9; no longer BANKB.30, BB_HIGH.3
- net DATAB9: now also BANKB.10; no longer BANKB.32, BB_HIGH.4
- net DATAC0: now also BANKC.1; no longer BANKC.29, BC_LOW.3
- net DATAC1: now also BANKC.2; no longer BANKC.31, BC_LOW.4
- net DATAC10: now also BANKC.11; no longer BANKC.34, BC_HIGH.5
- net DATAC11: now also BANKC.12; no longer BANKC.36, BC_HIGH.6
- net DATAC12: now also BANKC.13; no longer BANKC.39, BC_HIGH.10
- net DATAC13: now also BANKC.14; no longer BANKC.41, BC_HIGH.11
- net DATAC14: now also BANKC.15; no longer BANKC.43, BC_HIGH.12
- net DATAC15: now also BANKC.16; no longer BANKC.45, BC_HIGH.13
- net DATAC2: now also BANKC.3; no longer BANKC.33, BC_LOW.5
- net DATAC3: now also BANKC.4; no longer BANKC.35, BC_LOW.6
- net DATAC4: now also BANKC.5; no longer BANKC.38, BC_LOW.10
- net DATAC5: now also BANKC.6; no longer BANKC.40, BC_LOW.11
- net DATAC6: now also BANKC.7; no longer BANKC.42, BC_LOW.12
- net DATAC7: now also BANKC.8; no longer BANKC.44, BC_HIGH.1, BC_HIGH.2, BC_LOW.13
- net DATAC8: now also BANKC.9; no longer BANKC.30, BC_HIGH.3
- net DATAC9: now also BANKC.10; no longer BANKC.32, BC_HIGH.4
- net GND: now also SV2.2, SV2.3; no longer ADD_HIGH.7, ADD_LOW.7, ADD_MID.7, BANKA.26, BANKA.37, BANKB.26, BANKB.37, BANKC.26, BANKC.37, BA_HIGH.7, BA_LOW.7, BB_HIGH.7, BB_LOW.7, BC_HIGH.7, BC_LOW.7, JP3.11, READ_WRITE.3, SW_PROD_1.15, SW_PROD_1.8, SW_PROD_2.15, SW_PROD_2.8, SW_PROD_3.15, SW_PROD_3.8, SW_PROD_4.15, SW_PROD_4.8, SW_PROD_5.15, SW_PROD_5.8
- net IN_BUS0: now also JP3.20; no longer SW_PROD_1.14
- net IN_BUS1: now also JP3.10; no longer SW_PROD_1.11
- net IN_BUS10: now also JP3.15; no longer SW_PROD_3.5
- net IN_BUS11: now also JP3.5; no longer SW_PROD_3.2
- net IN_BUS12: now also JP3.14; no longer SW_PROD_4.2
- net IN_BUS13: now also JP3.4; no longer SW_PROD_4.5
- net IN_BUS14: now also JP3.13; no longer SW_PROD_4.11
- net IN_BUS15: now also JP3.3; no longer SW_PROD_4.14
- net IN_BUS16: now also JP3.12; no longer SW_PROD_5.2
- net IN_BUS17: now also JP3.2; no longer SW_PROD_5.5
- net IN_BUS18: now also JP3.11; no longer SW_PROD_5.11
- net IN_BUS19: now also JP3.1; no longer SW_PROD_5.14
- net IN_BUS2: now also JP3.19; no longer SW_PROD_1.5
- net IN_BUS3: now also JP3.9; no longer SW_PROD_1.2
- net IN_BUS4: now also JP3.18; no longer SW_PROD_2.14
- net IN_BUS5: now also JP3.8; no longer SW_PROD_2.11
- net IN_BUS6: now also JP3.17; no longer SW_PROD_2.5
- net IN_BUS7: now also JP3.7; no longer SW_PROD_2.2
- net IN_BUS8: now also JP3.16; no longer SW_PROD_3.14
- net IN_BUS9: now also JP3.6; no longer SW_PROD_3.11
- net VCC: now also SV2.1, SV2.4, SV2.5, SV2.6; no longer ADD_HIGH.14, ADD_LOW.14, ADD_MID.14, BA_HIGH.14, BA_LOW.14, BB_HIGH.14, BB_LOW.14, BC_HIGH.14, BC_LOW.14, JP3.12, R12.2, R13.2, R14.2, READ_WRITE.1, SW_PROD_1.16, SW_PROD_2.16, SW_PROD_3.16, SW_PROD_4.16, SW_PROD_5.16
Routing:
- net PROG_CLEAR: track 269.6 -> 0.00 mm, vias 8 -> 0
- net DATA_ADDR_CLOCK: track 265.0 -> 0.00 mm, vias 9 -> 0
- net ADDR_SHIFT: track 210.1 -> 0.00 mm, vias 1 -> 0
- net GND: track 711.5 -> 506.9 mm, vias 25 -> 16
- net !CLEAR: track 263.6 -> 61.2 mm, vias 6 -> 1
- net VCC: track 820.8 -> 630.4 mm, vias 23 -> 26
- net PROG_ADDR_CLOCK: track 180.8 -> 0.00 mm, vias 3 -> 0
- net DATAA_SHIFT: track 175.7 -> 0.00 mm
- net N$61: track 233.1 -> 399.4 mm, vias 4 -> 8
- net ADDR_BUS12: track 162.6 -> 0.00 mm
- net ADDR_BUS1: track 157.2 -> 0.00 mm, vias 4 -> 0
- net DATAC_SHIFT: track 152.6 -> 0.00 mm, vias 4 -> 0
- net PROG_DIR: track 150.6 -> 0.00 mm, vias 6 -> 0
- net ADDR_BUS3: track 135.1 -> 0.00 mm, vias 4 -> 0
- net DATAC4: track 176.0 -> 41.0 mm, vias 4 -> 0
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
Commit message: Finished All Boards
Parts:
- added C1, C2, C3, C4: 1uF, rcl:C1206
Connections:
- net GND: now also C1.2, C2.2, C3.2, C4.2
- net VCC: now also C1.1, C2.1, C3.1, C4.1
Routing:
- net VCC: track 630.4 -> 702.9 mm, vias 26 -> 28
- net GND: track 506.9 -> 574.6 mm, vias 16 -> 19

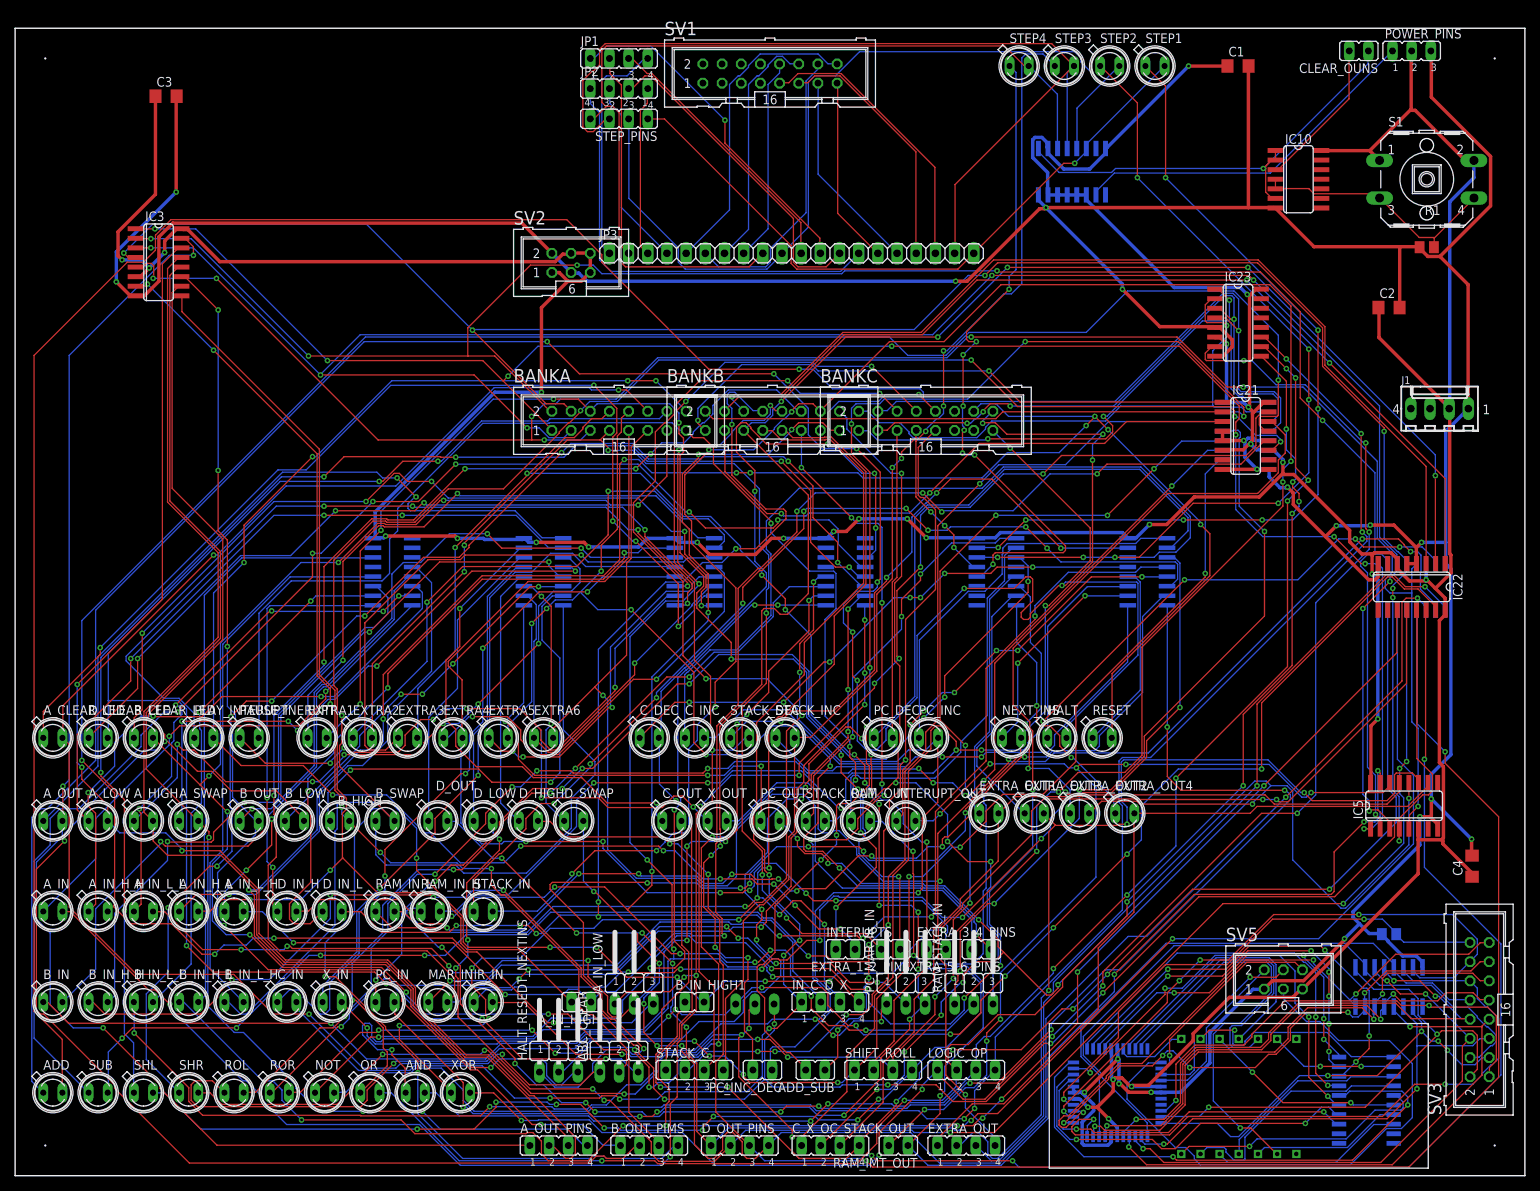
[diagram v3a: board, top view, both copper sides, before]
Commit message: Check in the changes to the Controller
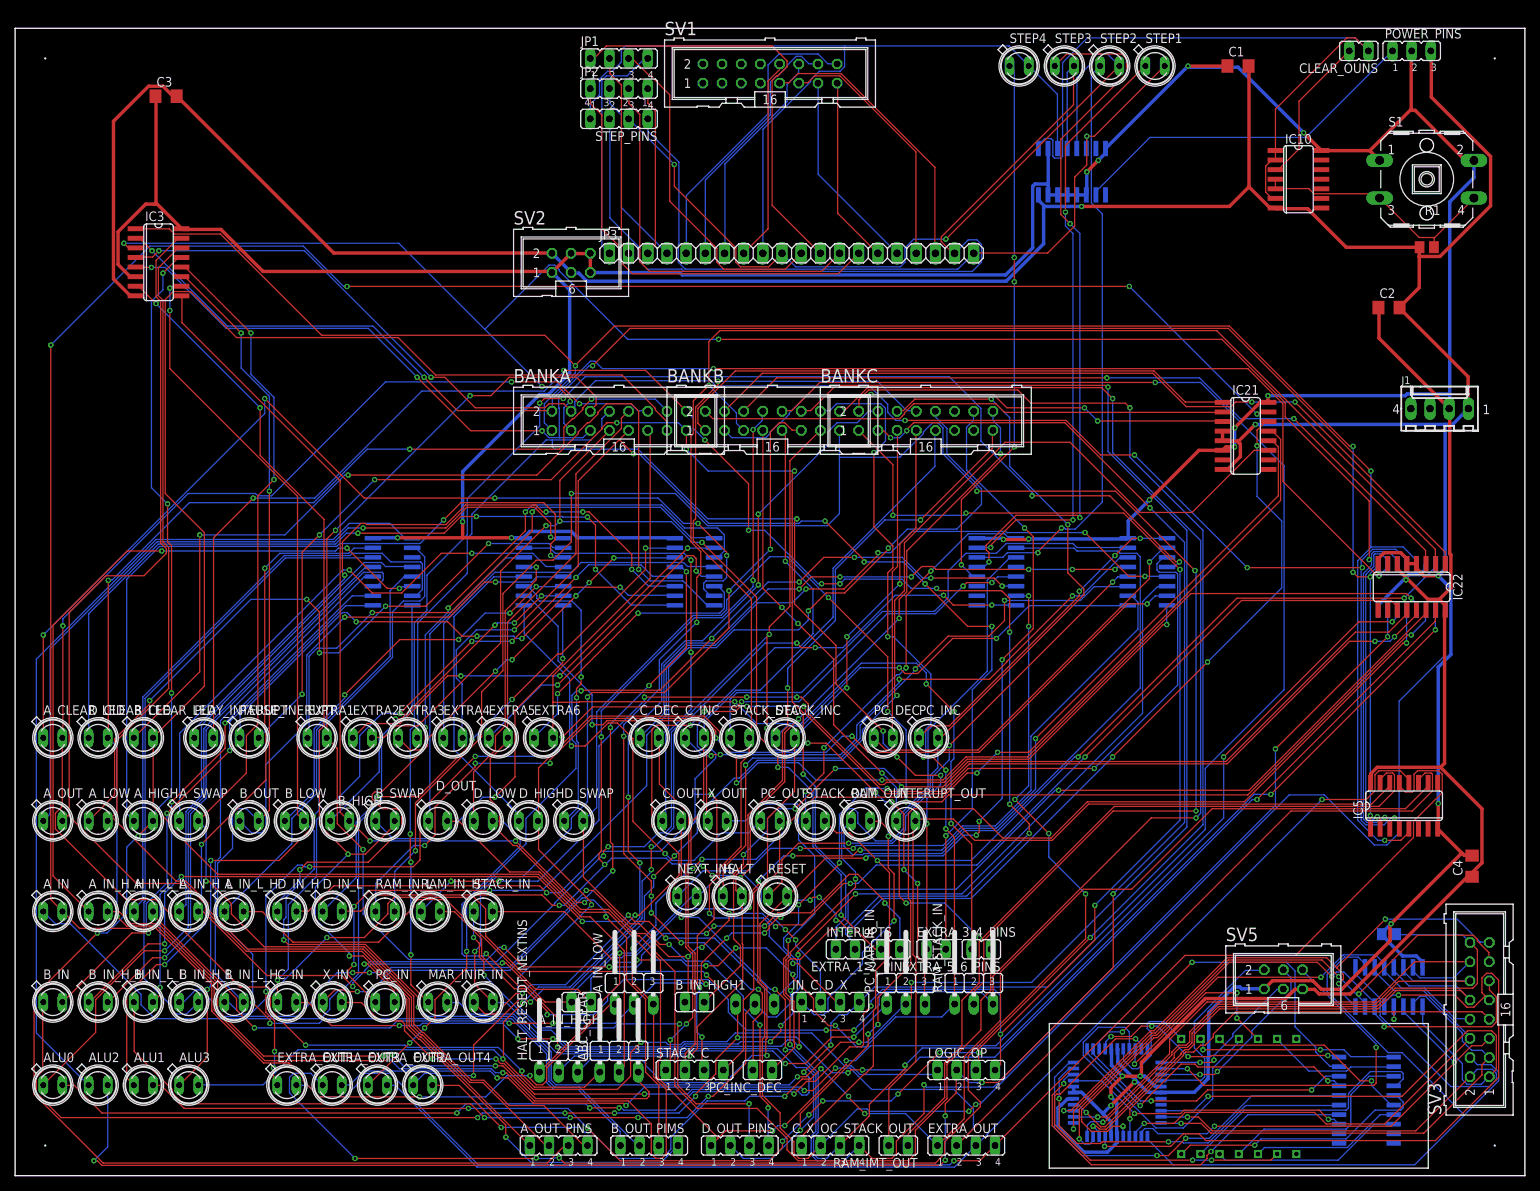
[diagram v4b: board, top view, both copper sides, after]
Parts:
- removed ADD, AND, NOT, OR, ROL, ROR, SHL, SHR, SUB, XOR: (no value), led:SFH482
- removed ADD_SUB: (no value), jumper:JP1
- removed IC1, IC23: 74LS138D, 74xx-us:SO16
- removed R7: (no value), resistor-bourns:SO16
- removed SHIFT_ROLL: (no value), jumper:JP4
- added ALU0, ALU1, ALU2, ALU3: (no value), led:SFH482
- moved EXTRA_OUT1 99.7 mm to (36.0, 12.0)
- moved EXTRA_OUT2 99.7 mm to (48.0, 12.0)
- moved EXTRA_OUT3 99.7 mm to (42.0, 12.0)
- moved EXTRA_OUT4 99.7 mm to (54.0, 12.0)
- moved HALT 47.9 mm to (95.0, 37.0)
- moved NEXT_INS 47.9 mm to (89.0, 37.0)
- moved RESET 47.9 mm to (101.0, 37.0)
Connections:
- removed net N$55: R7.8, ROR.A
- removed net N$56: R7.7, ROL.A
- removed net N$57: R7.6, SHR.A
- removed net N$58: R7.5, SHL.A
- removed net N$59: R7.4, SUB.A
- removed net N$60: ADD.A, R7.3
- removed net N$61: ADD.K, ADD_SUB.2, IC1.15
- removed net N$62: ADD_SUB.1, IC1.14, SUB.K
- removed net N$63: IC1.13, SHIFT_ROLL.4, SHL.K
- removed net N$64: IC1.12, SHIFT_ROLL.3, SHR.K
- removed net N$65: IC1.11, ROL.K, SHIFT_ROLL.2
- removed net N$66: IC1.10, ROR.K, SHIFT_ROLL.1
- removed net N$71: IC23.7, LOGIC_OP.1, XOR.K
- removed net N$72: IC23.9, LOGIC_OP.2, OR.K
- removed net N$73: AND.K, IC23.10, LOGIC_OP.3
- removed net N$74: IC23.11, LOGIC_OP.4, NOT.K
- new net N$37: IC5.6
- net DATAC0: now also ALU0.K, LOGIC_OP.4; no longer IC1.1, IC23.1
- net DATAC1: now also ALU1.K, LOGIC_OP.3; no longer IC1.2, IC23.2
- net DATAC2: now also ALU2.K, LOGIC_OP.2; no longer IC1.3, IC23.3
- net DATAC3: now also ALU3.K, LOGIC_OP.1; no longer IC1.4, IC23.4
- net GND: no longer IC1.5, IC1.8, IC23.5, IC23.8
- net N$67: now also ALU0.A, R4.13; no longer NOT.A, R7.9
- net N$68: now also ALU1.A, R4.15; no longer AND.A, R7.10
- net N$69: now also ALU2.A, R4.1; no longer OR.A, R7.11
- net N$70: now also ALU3.A, R4.2; no longer R7.12, XOR.A
- net VCC: no longer IC1.16, IC1.6, IC23.16, IC23.6, IC5.6, R7.16
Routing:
- net N$61: track 399.4 -> 0.00 mm, vias 8 -> 0
- net N$62: track 239.4 -> 0.00 mm, vias 10 -> 0
- net N$65: track 231.9 -> 0.00 mm, vias 11 -> 0
- net N$63: track 224.6 -> 0.00 mm, vias 12 -> 0
- net N$74: track 223.4 -> 0.00 mm, vias 5 -> 0
- net N$71: track 221.1 -> 0.00 mm, vias 9 -> 0
- net N$64: track 220.3 -> 0.00 mm, vias 12 -> 0
- net N$72: track 208.8 -> 0.00 mm, vias 8 -> 0
- net N$60: track 207.8 -> 0.00 mm, vias 4 -> 0
- net N$73: track 195.0 -> 0.00 mm, vias 9 -> 0
- net DATAC0: track 79.2 -> 272.6 mm, vias 3 -> 10
- net DATAC2: track 80.5 -> 273.2 mm, vias 4 -> 8
- net N$66: track 189.5 -> 0.00 mm, vias 10 -> 0
- net DATAC1: track 76.3 -> 263.1 mm, vias 1 -> 10
- net N$58: track 183.6 -> 0.00 mm, vias 6 -> 0
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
